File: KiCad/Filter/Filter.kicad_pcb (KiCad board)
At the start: 2 copper layers, 32 parts, among them J1 Screw_Terminal_01x03, J2 Screw_Terminal_01x03, U1 TL074

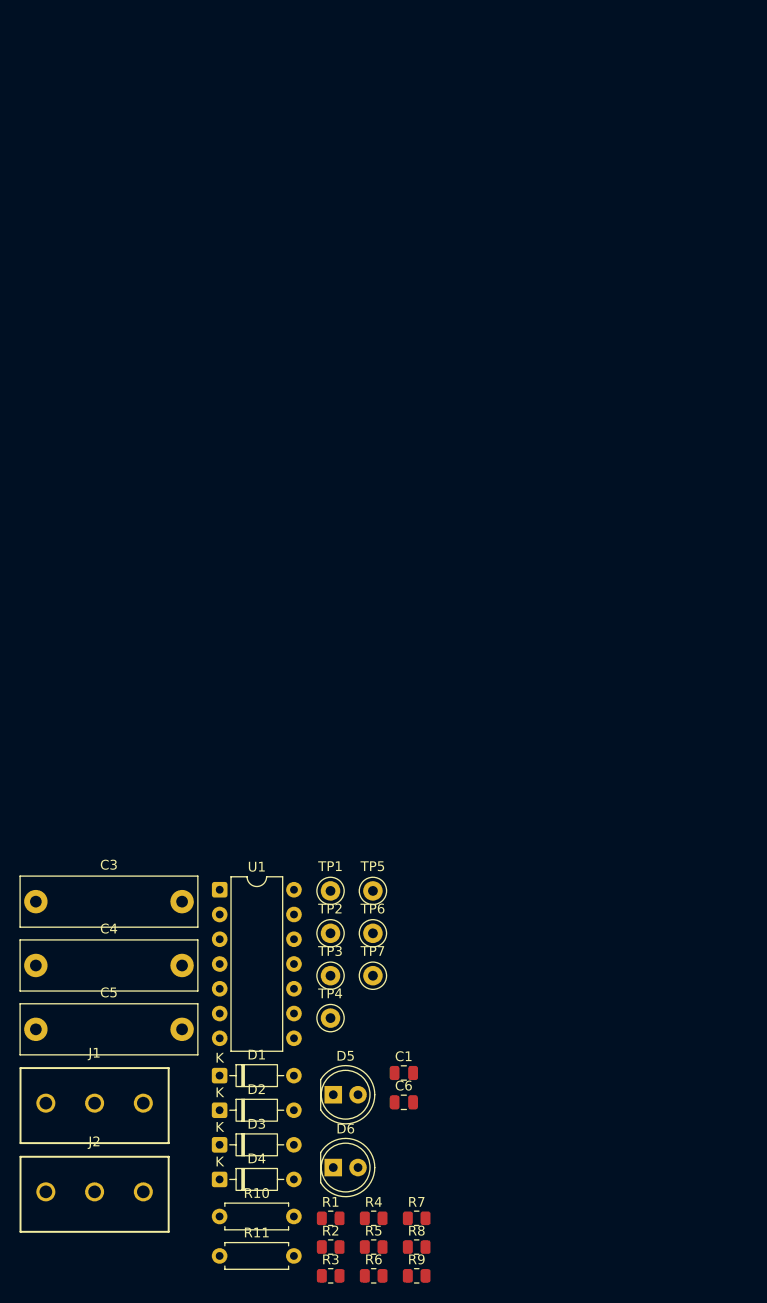
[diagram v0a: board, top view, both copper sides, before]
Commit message: filter pcb layout done
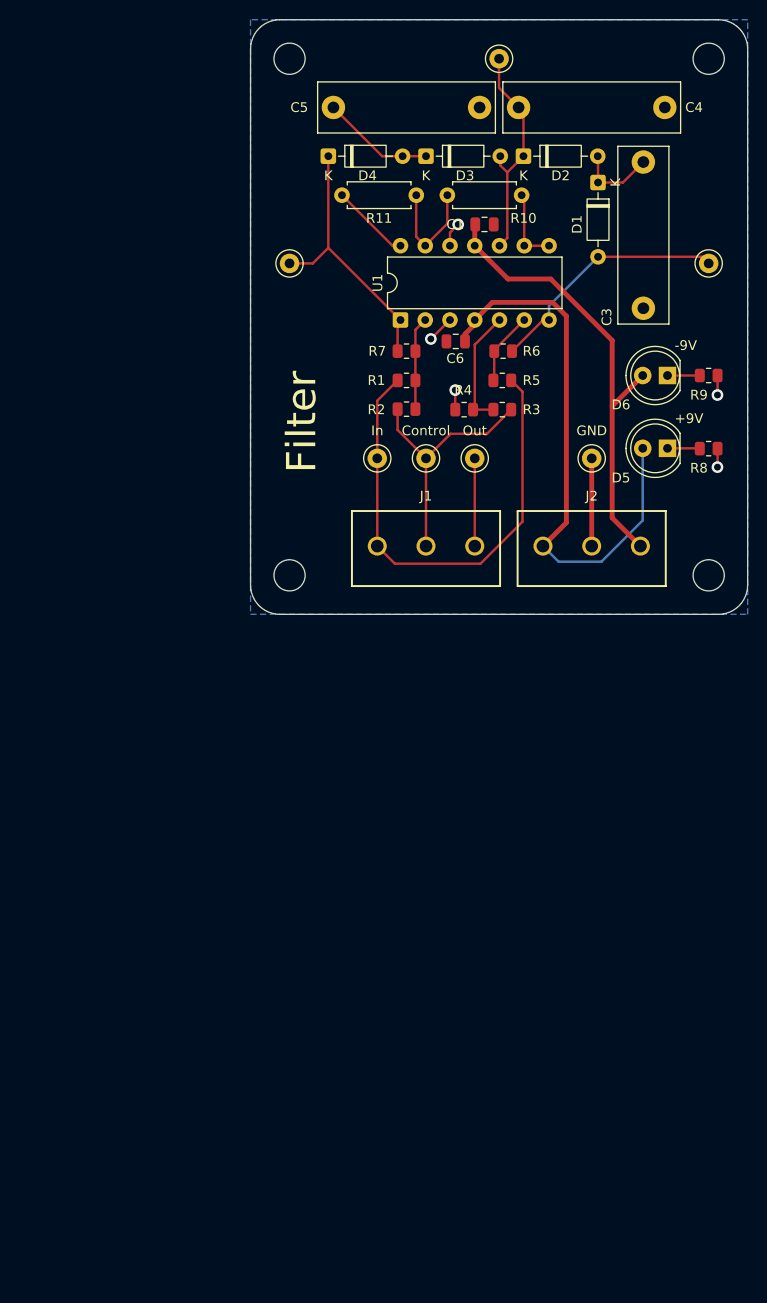
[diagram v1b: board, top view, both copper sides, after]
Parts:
- added REF**: MountingHole_3.2mm_M3, MountingHole:MountingHole_3.2mm_M3, F.Cu at (114.0, 101.0)
- added REF**: MountingHole_3.2mm_M3, MountingHole:MountingHole_3.2mm_M3, F.Cu at (71.0, 101.0)
- added REF**: MountingHole_3.2mm_M3, MountingHole:MountingHole_3.2mm_M3, F.Cu at (71.0, 48.0)
- added REF**: MountingHole_3.2mm_M3, MountingHole:MountingHole_3.2mm_M3, F.Cu at (114.0, 48.0)
- moved R11 110.7 mm to (84.0, 62.0), turned to 180 degrees
- moved R10 109.3 mm to (94.8, 62.0), turned to 180 degrees
- moved C4 109.1 mm to (109.5, 53.0), turned to 180 degrees
- moved D4 105.6 mm to (75.0, 58.0)
- moved C5 105.0 mm to (90.5, 53.0), turned to 180 degrees
- moved D3 103.6 mm to (85.0, 58.0)
- moved D2 102.7 mm to (95.0, 58.0)
- moved D1 99.5 mm to (102.7, 60.7), turned to -90 degrees
- moved R9 97.1 mm to (114.0, 80.5)
- moved R6 95.8 mm to (92.9, 78.0)
- moved TP7 95.0 mm to (92.5, 48.0)
- moved R3 90.6 mm to (92.8, 84.0)
- moved R5 89.9 mm to (92.8, 81.0), turned to 180 degrees
- moved R7 89.0 mm to (83.0, 78.0), turned to 180 degrees
- moved D6 88.2 mm to (109.8, 80.5), turned to 180 degrees
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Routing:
- net +9V: track 0.00 -> 58.0 mm
- net /In: track 0.00 -> 50.3 mm
- net -9V: track 0.00 -> 47.1 mm
- net /Signal w. - Offset: track 0.00 -> 27.8 mm
- net /Control: track 0.00 -> 26.1 mm
- net /Signal w. + Offset: track 0.00 -> 25.3 mm
- net /Inverted Raw Out: track 0.00 -> 23.2 mm
- net GND: track 0.00 -> 20.2 mm, vias 0 -> 5
- net /Out: track 0.00 -> 17.1 mm
- net Net-(U1B-+): track 0.00 -> 12.4 mm
- net Net-(U1D--): track 0.00 -> 11.7 mm
- net Net-(D3-K): track 0.00 -> 11.6 mm
- net Net-(U1A--): track 0.00 -> 9.56 mm
- net Net-(D1-K): track 0.00 -> 8.23 mm
- net /Buffered Inverted Raw Out: track 0.00 -> 7.84 mm
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- added copper zone on B.Cu, net GND
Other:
- board outline added: 51 x 61 mm
- board text added: "+9V"
- board text added: "-9V"
- board text added: "Control"
- board text added: "Filter"
- board text added: "GND"
- board text added: "In"
- board text added: "Out"

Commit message: power pcb layout done
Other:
- board text added: "Inverted, Raw Out"
- board text added: "Neg Offset In"
- board text added: "Pos Offset In"
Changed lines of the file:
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@@
 		(layer "Edge.Cuts")
 	)
-	(gr_text "-9V"
-		(at 110.5 78 0)
+	(gr_text "Neg\nOffset In"
+		(at 69 75.25 0)
 		(layer "F.SilkS")
 		(effects
 			(font
-				(size 1 1)
-				(thickness 0.15)
+				(size 1.5 1.5)
+				(thickness 0.3)
+				(bold yes)
+			)
+			(justify left bottom)
+		)
+	)
+	(gr_text "-9V"
+		(at 111.5 78.75 0)
+		(layer "F.SilkS")
+		(effects
+			(font
+				(size 1.5 1.5)
+				(thickness 0.3)
+				(bold yes)
 			)
 			(justify left bottom)
@@
 	)
 	(gr_text "+9V"
-		(at 110.5 85.5 0)
+		(at 111.5 86.25 0)
 		(layer "F.SilkS")
 		(effects
 			(font
-				(size 1 1)
-				(thickness 0.15)
+				(size 1.5 1.5)
+				(thickness 0.3)
+				(bold yes)
 			)
 			(justify left bottom)
@@
 	)
 	(gr_text "In"
-		(at 80 86.75 0)
+		(at 77 90 0)
 		(layer "F.SilkS")
 		(effects
 			(font
-				(size 1 1)
-				(thickness 0.15)
+				(size 1.5 1.5)
+				(thickness 0.3)
+				(bold yes)
 			)
 			(justify bottom)
@@
 	)
 	(gr_text "Control"
-		(at 85 86.75 0)
+		(at 85 87.25 0)
 		(layer "F.SilkS")
 		(effects
 			(font
-				(size 1 1)
-				(thickness 0.15)
+				(size 1.5 1.5)
+				(thickness 0.3)
+				(bold yes)
+			)
+			(justify bottom)
+		)
+	)
+	(gr_text "Inverted,    Raw Out"
+		(at 92.5 48.5 0)
+		(layer "F.SilkS")
+		(effects
+			(font
+				(size 1.5 1.5)
+				(thickness 0.3)
+				(bold yes)
 			)
 			(justify bottom)
@@
 	)
 	(gr_text "Out"
-		(at 90 86.75 0)
+		(at 94 90 0)
 		(layer "F.SilkS")
 		(effects
 			(font
-				(size 1 1)
-				(thickness 0.15)
+				(size 1.5 1.5)
+				(thickness 0.3)
+				(bold yes)
 			)
 			(justify bottom)
@@
 	)
 	(gr_text "GND"
-		(at 102 86.75 0)
+		(at 102 87.25 0)
 		(layer "F.SilkS")
 		(effects
 			(font
-				(size 1 1)
-				(thickness 0.15)
+				(size 1.5 1.5)
+				(thickness 0.3)
+				(bold yes)
 			)
 			(justify bottom)
 		)
 	)
-	(gr_text "Filter"
-		(at 74 90.5 90)
+	(gr_text "Pos\nOffset\nIn"
+		(at 117 67 0)
 		(layer "F.SilkS")
 		(effects
 			(font
-				(size 3 3)
-				(thickness 0.45)
+				(size 1.5 1.5)
+				(thickness 0.3)
+				(bold yes)
+			)
+			(justify right bottom)
+		)
+	)
+	(gr_text "Filter"
+		(at 73.75 94 90)
+		(layer "F.SilkS")
+		(effects
+			(font
+				(size 3.5 3.5)
+				(thickness 0.7)
+				(bold yes)
 			)
 			(justify left bottom)

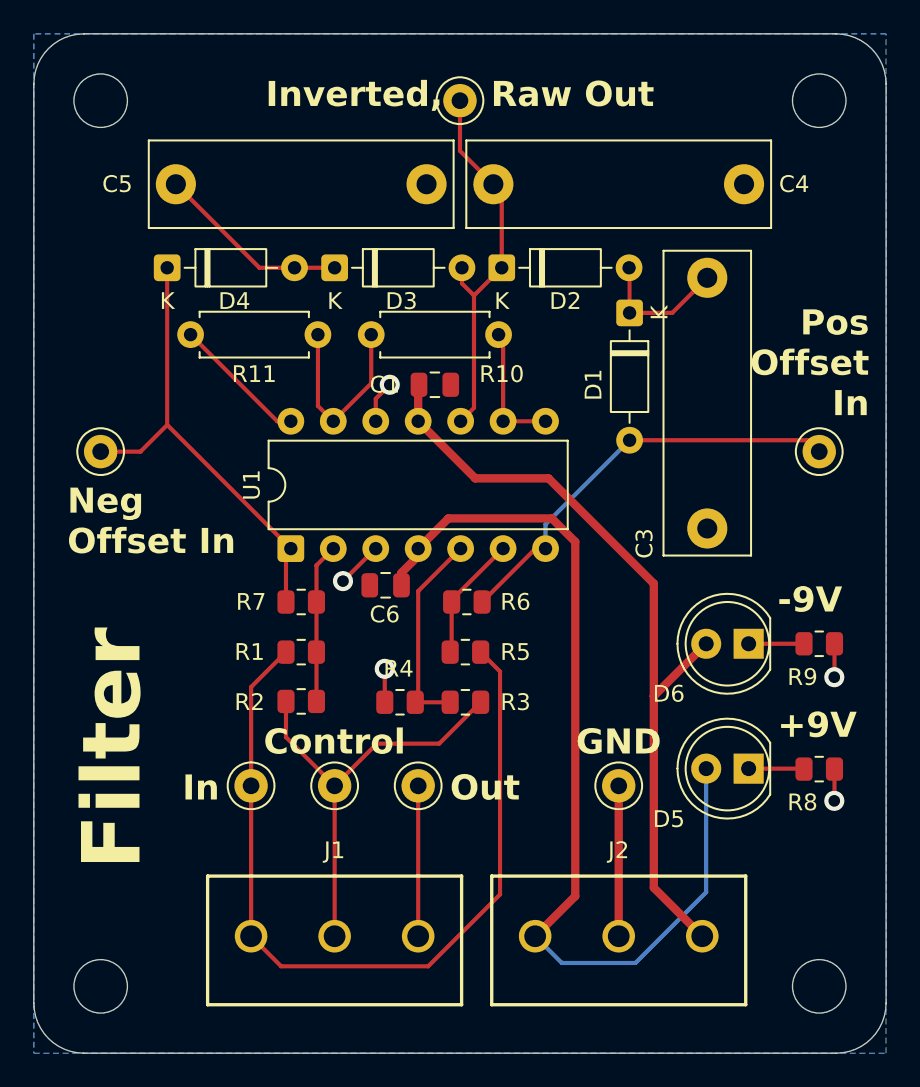
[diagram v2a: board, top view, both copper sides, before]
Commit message: added mounting holes to schematics, adjusted board sizes
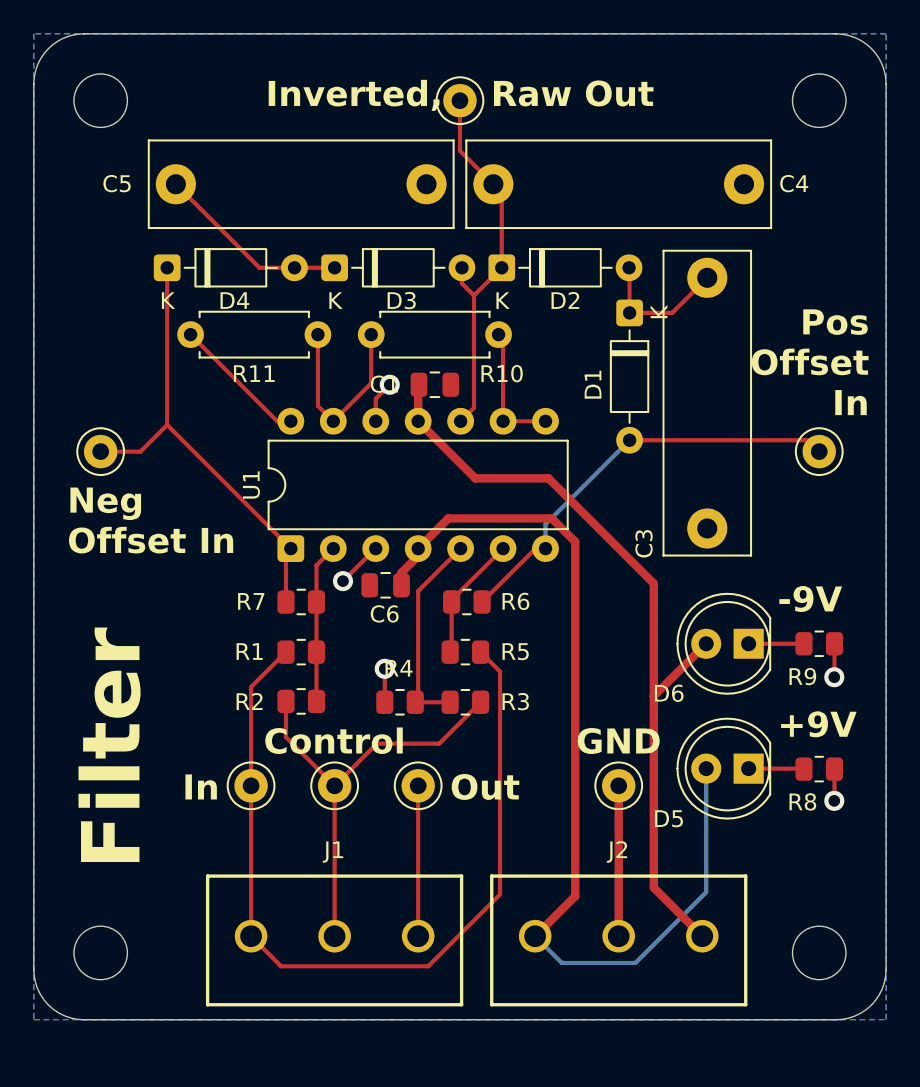
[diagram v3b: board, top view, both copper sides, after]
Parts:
- moved H2 2.00 mm to (71.0, 99.0)
- moved H3 2.00 mm to (114.0, 99.0)
- renumbered REF** to H1, REF** to H2, REF** to H3, REF** to H4
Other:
- board size 51 x 61 mm -> 51 x 59 mm
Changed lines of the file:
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@@
 	(footprint "MountingHole:MountingHole_3.2mm_M3"
 		(layer "F.Cu")
-		(at 114 101)
+		(at 114 99)
 		(descr "Mounting Hole 3.2mm, M3, no annular, generated by kicad-footprint-generator mountinghole.py")
 		(tags "mountinghole M3")
-		(property "Reference" "REF**"
+		(property "Reference" "H3"
 			(at 0 -4.15 0)
 			(layer "F.SilkS")
@@
 	(footprint "MountingHole:MountingHole_3.2mm_M3"
 		(layer "F.Cu")
-		(at 71 101)
+		(at 71 99)
 		(descr "Mounting Hole 3.2mm, M3, no annular, generated by kicad-footprint-generator mountinghole.py")
 		(tags "mountinghole M3")
-		(property "Reference" "REF**"
+		(property "Reference" "H2"
 			(at 0 -4.15 0)
 			(layer "F.SilkS")
@@
 		(descr "Mounting Hole 3.2mm, M3, no annular, generated by kicad-footprint-generator mountinghole.py")
 		(tags "mountinghole M3")
-		(property "Reference" "REF**"
+		(property "Reference" "H1"
 			(at 0 -4.15 0)
 			(layer "F.SilkS")
@@
 		(descr "Mounting Hole 3.2mm, M3, no annular, generated by kicad-footprint-generator mountinghole.py")
 		(tags "mountinghole M3")
-		(property "Reference" "REF**"
+		(property "Reference" "H4"
 			(at 0 -4.15 0)
 			(layer "F.SilkS")
@@
 	)
 	(gr_line
-		(start 67 102)
+		(start 67 100)
 		(end 67 47)
 		(stroke
@@
 	)
 	(gr_arc
-		(start 70 105)
-		(mid 67.87868 104.12132)
-		(end 67 102)
+		(start 70 103)
+		(mid 67.87868 102.12132)
+		(end 67 100)
 		(stroke
 			(width 0.05)
@@
 	)
 	(gr_line
-		(start 115 105)
-		(end 70 105)
+		(start 115 103)
+		(end 70 103)
 		(stroke
 			(width 0.05)
@@
 	)
 	(gr_arc
-		(start 117.999954 101.999996)
-		(mid 117.121274 104.121316)
-		(end 114.999954 104.999996)
+		(start 117.999954 99.999996)
+		(mid 117.121274 102.121316)
+		(end 114.999954 102.999996)
 		(stroke
 			(width 0.05)
@@
 	)
 	(gr_line
-		(start 118 102)
+		(start 118 100)
 		(end 117.999997 47.000003)
 		(stroke
@@
 		(polygon
 			(pts
-				(xy 67 44) (xy 67 105) (xy 118 105) (xy 118 44)
+				(xy 67 44) (xy 67 103) (xy 118 103) (xy 118 44)
 			)
 		)
